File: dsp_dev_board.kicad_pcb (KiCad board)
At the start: 4 copper layers, 100 x 100 mm, 85 parts, among them J1 aux_mcu_power, J10 DX07S016JA1R1500, J2 audio_in, J3 audio_out, J4 9v_jack, J5 input_jack, J6 output_jack, J7 digital, J8 analog, J9 debug, U1 TL072, U2 AMS1117-3.3, U3 ATSAME51J18A-A, U4 WM8731SEDS, U5 TLV320AIC3105IRHBR, U6 AMS1117-1.8, Y1 8Mhz

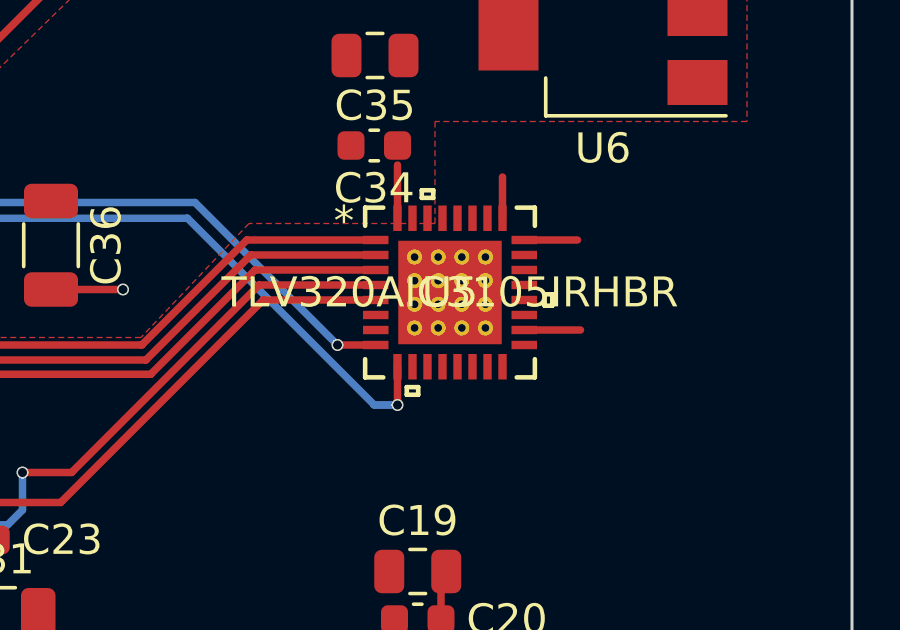
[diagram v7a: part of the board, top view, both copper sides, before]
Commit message: PCB: update TI's footprint so thermal vias are GND
They were numbered "V" which KiCad thought should be a different net,
throwing all sorts of DRC errors.  Numbering them all 33 makes it act
like the built-in footprint with thermal vias.
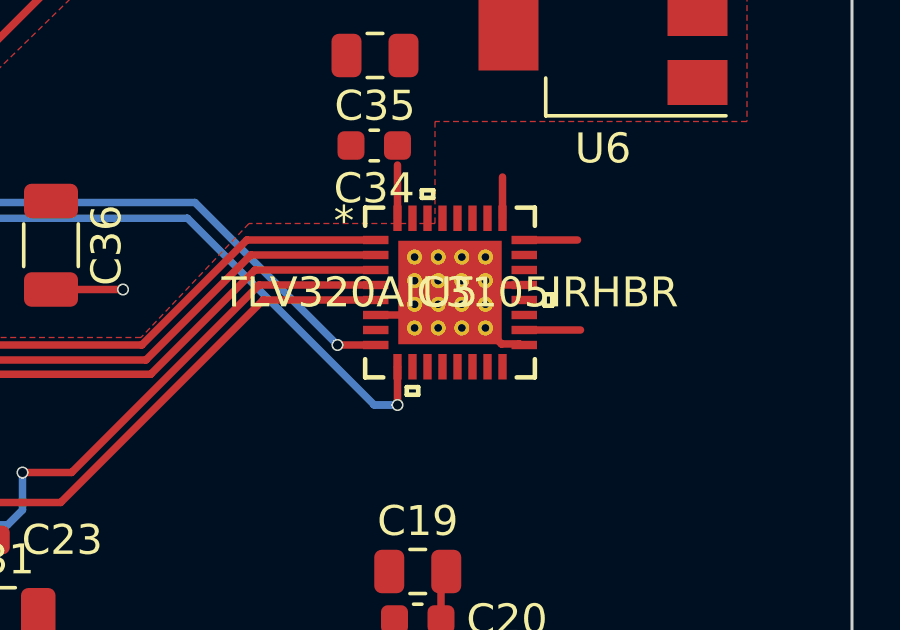
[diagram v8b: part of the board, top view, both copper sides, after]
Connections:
- C17 pad 2: Net-(C17-Pad2) -> GND
- C19 pad 2: Net-(C17-Pad2) -> GND
- C20 pad 2: Net-(C17-Pad2) -> GND
- C25 pad 2: Net-(C17-Pad2) -> GND
- C26 pad 2: Net-(C17-Pad2) -> GND
- C27 pad 2: Net-(C17-Pad2) -> GND
- C28 pad 2: Net-(C17-Pad2) -> GND
- C33 pad 2: Net-(C17-Pad2) -> GND
- C34 pad 2: Net-(C17-Pad2) -> GND
- C35 pad 2: Net-(C17-Pad2) -> GND
- U4 pad 12: /audio_out -> /Codec/audio_out
- U4 pad 20: /audio_in -> /Codec/audio_in
- U5 pad 10: /audio_in -> /TI Codec/audio_in
- U5 pad 27: /audio_out -> /TI Codec/audio_out
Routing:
- net GND: track 79.8 -> 90.0 mm
- net Net-(C17-Pad2): track 1.60 -> 0.00 mm
